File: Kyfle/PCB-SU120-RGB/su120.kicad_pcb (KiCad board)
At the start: 2 copper layers, 94 x 94 mm, 416 parts, among them J1 MJ-4PP-9, J2 Conn_01x03, J3 Conn_01x08, J4 Conn_01x08, J6 MJ-4PP-9, J7 Conn_02x05_Odd_Even, J8 Conn_02x05_Odd_Even, SW1 SW_PUSH_LED, SW10 SW_PUSH_LED, SW11 SW_PUSH_LED, SW12 SW_PUSH_LED, SW13 SW_PUSH_LED, SW14 SW_PUSH_LED, SW15 SW_PUSH_LED, SW16 SW_PUSH_LED, SW17 SW_PUSH_LED, SW18 SW_PUSH_LED, SW2 SW_PUSH_LED, SW20 Rotary_Encoder_Switch, SW21 Rotary_Encoder_Switch, SW22 SW_Push, SW3 SW_PUSH_LED, SW4 SW_PUSH_LED, SW5 SW_PUSH_LED, SW6 SW_PUSH_LED, SW7 SW_PUSH_LED, SW8 SW_PUSH_LED, SW9 SW_PUSH_LED, U1 ProMicro

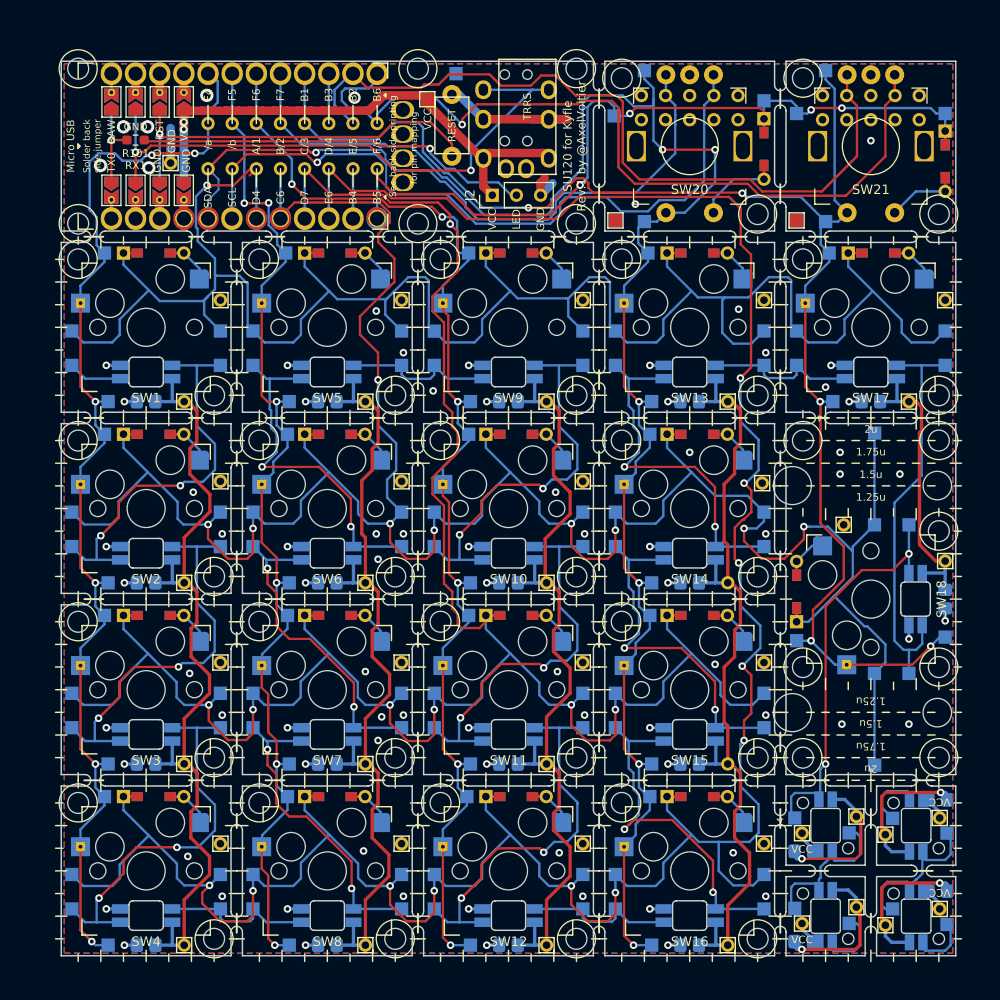
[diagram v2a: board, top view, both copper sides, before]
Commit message: Massive redesign
- Realised the design was not reversible. Only solution was to mirror the two diagonal holes of each bit. But one of them was coliding with hotswap socket footprint. Until...
- I also realised that having the holes at these Y positions made the screw coming on top collide with the bottom of the switch housing...
- So switched to having two holes right in between each bit (vertically).
- Then I realised cheap pcb houses can have quite some limitations when it comes to exotic uses of slots. In particular, for jlcpcb:
  * They prefer tabs to be >= 4mm wide
  * They prefer at least 3mm of PCB next to a slot (ie. avoid slim inter-slots parts)
  * They prefer 0.4mm clearence from board edge when it is milled/routed
  * Watching some videos of their fab it seems they do the edge.cuts routing with a single 1mm bit. Ie. if you specify a larger radius they actually route it out. And if you specify a smaller radius (than 0.5mm) they cannot do it.

So, I redid the PCB. Twice... Again. For now...

I also started reorganising the projects. First part was to gather all footprints used accross the three boards. Makes cross-board editing of footprints easier.
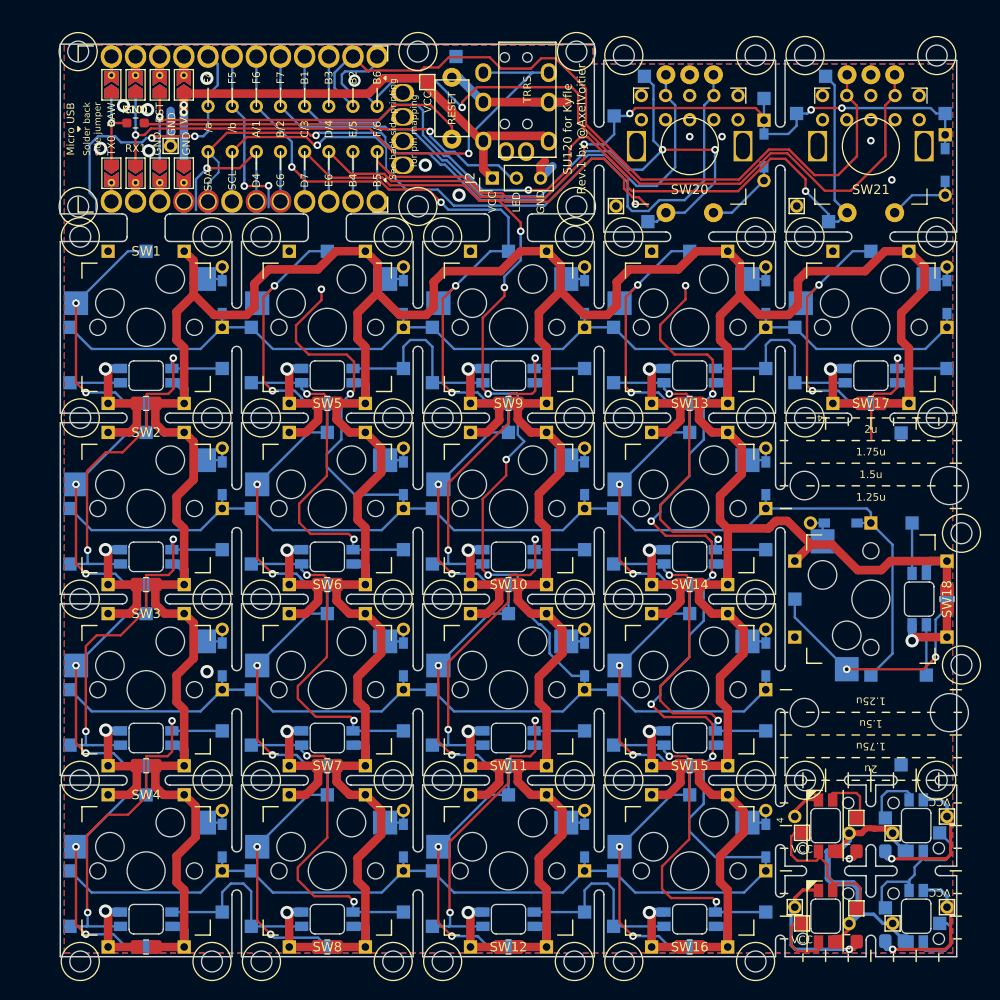
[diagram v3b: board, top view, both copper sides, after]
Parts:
- removed the ? at (120.7, 135.7)
- removed the ? at (134.9, 73.8)
- removed the ? at (120.7, 59.5)
- removed the ? at (101.6, 59.5)
- removed the ? at (70.6, 85.7)
- removed the ? at (89.7, 142.9)
- removed the ? at (108.7, 142.9)
- removed the ? at (127.8, 114.3)
- removed the ? at (51.6, 123.8)
- removed the ? at (70.6, 123.8)
- removed the ? at (89.7, 123.8)
- removed the ? at (108.7, 123.8)
- removed the ? at (70.6, 142.9)
- removed the ? at (51.6, 142.9)
- removed the ? at (108.7, 104.8)
- removed the ? at (89.7, 104.8)
- removed the ? at (70.6, 104.8)
- removed the ? at (51.6, 104.8)
- removed the ? at (51.6, 85.7)
- removed the ? at (89.7, 85.7)
- removed the ? at (127.8, 85.7)
- removed the ? at (125.4, 140.5)
- removed the ? at (108.7, 85.7)
- removed the ? at (80.6, 65.5)
- removed the ? at (83.7, 65.1)
- removed the ? at (125.4, 150.0)
- removed the ? at (120.7, 145.3)
- removed C1, C10, C11, C12, C13, C14, C15, C16, C17, C18, C2, C3, C4, C5, C6, C7, C8, C9: 100n, #footprint:C_0603_0805_HandSolder
- removed D1, D10, D11, D12, D13, D14, D15, D16, D17, D2, D20, D3, D4, D5, D6, D7, D8, D9: D, #footprint:diode_TH_SMD_rev2
- removed H1, H10, H100, H102, H104, H106, H108, H11, H110, H112, H113, H114, H115, H116, H117, H118, H119, H12, H120, H121, H122, H123, H124, H125, H126, H127, H128, H129, H13, H130, H131, H132, H14, H142, H145, H147, H149, H15, H151, H16, H17, H18, H19, H2, H20, H21, H210, H211, H212, H213, H22, H23, H24, H25, H26, H27, H28, H29, H3, H30, H31, H32, H33, H34, H35, H36, H37, H38, H39, H4, H40, H41, H42, H43, H44, H45, H47, H48, H49, H5, H51, H53, H55, H59, H6, H61, H63, H65, H67, H69, H7, H71, H72, H74, H76, H78, H8, H80, H82, H84, H87, H89, H9, H91, H93, H95, H97, H99: MountingHole_Pad, #footprint:1pad_conn
- removed H101, H103, H105, H107, H109, H111, H141, H143, H144, H146, H148, H150, H52, H54, H56, H58, H60, H62, H64, H66, H68, H70, H73, H75, H77, H79, H81, H83, H85, H86, H88, H90, H92, H94, H96, H98: MountingHole_Pad, #footprint:1pin_conn
- removed the REF** at (118.3, 66.7)
- removed the REF** at (80.2, 123.8)
- removed the REF** at (61.1, 123.8)
- removed the REF** at (61.1, 104.8)
- removed the REF** at (80.2, 104.8)
- removed the REF** at (99.2, 104.8)
- removed the REF** at (118.3, 85.7)
- removed the REF** at (99.2, 85.7)
- removed the REF** at (80.2, 85.7)
- removed the REF** at (61.1, 85.7)
- removed the REF** at (127.8, 95.2)
- removed the REF** at (99.2, 66.7)
- removed the REF** at (127.8, 76.2)
- removed the REF** at (108.7, 76.2)
- removed the REF** at (108.7, 95.2)
- removed the REF** at (108.7, 114.3)
- removed the REF** at (108.7, 133.3)
- removed the REF** at (89.7, 133.3)
- removed the REF** at (89.7, 114.3)
- removed the REF** at (89.7, 95.2)
- removed the REF** at (89.7, 76.2)
- removed the REF** at (70.6, 95.2)
- removed the REF** at (118.3, 104.8)
- removed the REF** at (70.6, 114.3)
- removed the REF** at (70.6, 133.3)
- removed the REF** at (51.6, 133.3)
- removed the REF** at (51.6, 114.3)
- removed the REF** at (51.6, 95.2)
- removed the REF** at (51.6, 76.2)
- removed the REF** at (118.3, 142.9)
- removed the REF** at (127.8, 133.3)
- removed the REF** at (127.8, 142.9)
- removed the REF** at (118.3, 123.8)
- removed the REF** at (70.6, 76.2)
- removed the REF** at (118.3, 133.3)
- removed the REF** at (118.3, 152.4)
- removed the REF** at (127.8, 152.4)
- removed the REF** at (61.1, 142.9)
- removed the REF** at (42.1, 95.2)
- removed the REF** at (80.2, 142.9)
- removed the REF** at (99.2, 142.9)
- removed the REF** at (99.2, 123.8)
- removed the Ref** at (134.9, 121.4)
- removed the Ref** at (82.5, 135.7)
- removed the Ref** at (101.6, 135.7)
- removed the Ref** at (101.6, 116.7)
- removed the Ref** at (82.5, 116.7)
- removed the Ref** at (63.5, 116.7)
- removed the Ref** at (44.5, 116.7)
- removed the Ref** at (44.5, 97.6)
- removed the Ref** at (63.5, 97.6)
- removed the Ref** at (82.5, 97.6)
- removed the Ref** at (101.6, 97.6)
- removed the Ref** at (134.9, 107.2)
- removed the Ref** at (120.7, 78.6)
- removed the Ref** at (101.6, 78.6)
- removed the Ref** at (82.5, 78.6)
- removed the Ref** at (63.5, 78.6)
- removed the Ref** at (44.5, 78.6)
- removed the Ref** at (58.7, 150.0)
- removed the Ref** at (77.8, 150.0)
- removed the Ref** at (96.8, 150.0)
- removed the Ref** at (115.9, 150.0)
- removed the Ref** at (115.9, 131.0)
- removed the Ref** at (120.7, 121.4)
- removed the Ref** at (96.8, 131.0)
- removed the Ref** at (77.8, 131.0)
- removed the Ref** at (58.7, 131.0)
- removed the Ref** at (58.7, 111.9)
- removed the Ref** at (77.8, 111.9)
- removed the Ref** at (96.8, 111.9)
- removed the Ref** at (115.9, 111.9)
- removed the Ref** at (134.9, 92.9)
- removed the Ref** at (115.9, 92.9)
- removed the Ref** at (96.8, 92.9)
- removed the Ref** at (120.7, 131.0)
- removed the Ref** at (77.8, 92.9)
- removed the Ref** at (58.7, 92.9)
- removed the Ref** at (134.9, 97.6)
- removed the Ref** at (120.7, 97.6)
- removed the Ref** at (44.5, 135.7)
- removed the Ref** at (63.5, 135.7)
- added ?: , Kyfle Footprints:M2_Hole_Standoff_Large_Cleareance, F.Cu at (115.7, 57.1)
- added ?: , Kyfle Footprints:M2_Hole_Standoff_Large_Cleareance, F.Cu at (120.9, 57.1)
- added ?: , Kyfle Footprints:M2_Hole_Standoff_Large_Cleareance, F.Cu at (134.7, 57.1)
- added ?: , Kyfle Footprints:M2_Hole_Standoff_Large_Cleareance, F.Cu at (134.7, 76.2)
- added ?: , Kyfle Footprints:M2_Hole_Standoff_Large_Cleareance, F.Cu at (120.9, 76.2)
- added ?: , Kyfle Footprints:M2_Hole_Standoff_Large_Cleareance, F.Cu at (101.8, 76.2)
- added ?: , Kyfle Footprints:M1.4_tapping_Hole, B.Cu at (120.7, 140.5)
- added ?: , Kyfle Footprints:M1.4_tapping_Hole, B.Cu at (120.7, 150.0)
- added ?: , Kyfle Footprints:M1.4_tapping_Hole, B.Cu at (125.4, 145.3)
- added ?: , Kyfle Footprints:M1.4_tapping_Hole, B.Cu at (125.4, 135.7)
- added ?: , Kyfle Footprints:M2_Hole_Standoff_Large_Cleareance, F.Cu at (96.6, 76.2)
- added ?: , , F.Cu at (80.6, 63.7)
- added ?: , , F.Cu at (83.7, 63.3)
- added ?: , Kyfle Footprints:M2_Hole_Standoff_Large_Cleareance, F.Cu at (82.8, 76.2)
- added ?: , Kyfle Footprints:M2_Hole_Standoff_Large_Cleareance, F.Cu at (77.6, 76.2)
- added ?: , Kyfle Footprints:M2_Hole_Standoff_Large_Cleareance, F.Cu at (63.7, 76.2)
- added ?: , Kyfle Footprints:M2_Hole_Standoff_Large_Cleareance, F.Cu at (58.5, 76.2)
- added ?: , Kyfle Footprints:M2_Hole_Standoff_Large_Cleareance, F.Cu at (44.7, 76.2)
- added ?: , Kyfle Footprints:M2_Hole_Standoff_Large_Cleareance, F.Cu at (101.8, 57.1)
- added REF**: Slot_1.2mm_9.75mm, Kyfle Footprints:Slot_Tee_1mm_2.7625mm, F.Cu at (127.8, 133.3)
- added REF**: Slot_1.2mm_9.75mm, Kyfle Footprints:Slot_Cross_1mm_2.7625mm, F.Cu at (127.8, 142.9)
- added REF**: Slot_1.2mm_3.7.mm, Kyfle Footprints:Slot_Half_Line_1mm_2.7625mm, F.Cu at (127.8, 152.4)
- added REF**: Slot_1.2mm_3.7.mm, Kyfle Footprints:Slot_Half_Line_1mm_2.7625mm, F.Cu at (118.3, 152.4)
- added REF**: Slot_1.2mm_3.7.mm, Kyfle Footprints:Slot_Half_Line_1mm_7.525mm, F.Cu at (42.1, 95.2)
- added REF** (x2): Slot_1.2mm_3.7.mm, Kyfle Footprints:Slot_Half_Line_1mm_2.7625mm, F.Cu at (118.3, 133.3)
- added REF** (x2): Slot_1.2mm_3.7.mm, Kyfle Footprints:Slot_Half_Line_1mm_7.525mm, F.Cu at (118.3, 133.3)
- added REF**: Slot_1.2mm_9.75mm, Kyfle Footprints:Slot_Tee_1mm_2.7625mm, F.Cu at (118.3, 142.9)
- added Ref**: Val**, Kyfle Footprints:M2_Hole_Standoff, F.Cu at (120.9, 133.3)
- ?: footprint #footprint:OLED_rivet -> Kyfle Footprints:OLED_Rivets
- ?: footprint #footprint:M2_Hole_Standoff -> Kyfle Footprints:M2_Hole_Standoff_Large_Cleareance
- ? (x4): footprint #footprint:M1.4_tapping_Hole -> Kyfle Footprints:M1.4_tapping_Hole
- ?: footprint #footprint:CherryMX_MidHeight_Choc_Hotswap_2U_Outline -> Kyfle Footprints:CherryMX_2U_Outline
- ? (x6), Ref**: footprint #footprint:M2_Hole_Standoff -> Kyfle Footprints:M2_Hole_Standoff
- ?: footprint #footprint:CherryMX_MidHeight_Choc_Silk -> Kyfle Footprints:CherryMX_MidHeight_Choc_Silk
- ? (x6): footprint #footprint:CherryMX_MidHeight_Choc_Silk_Line -> Kyfle Footprints:CherryMX_MidHeight_Choc_Silk_Line
- C19, C20: footprint #footprint:C_0603_0805_HandSolder -> Kyfle Footprints:C_0603_0805_HandSolder; moved to F.Cu
- C21, C22: footprint #footprint:C_0603_0805_HandSolder -> Kyfle Footprints:C_0603_0805_HandSolder
- D18, D19: footprint #footprint:diode_TH_SMD_rev2 -> Kyfle Footprints:diode_TH_SMD_rev3
- H133, H134, H135, H136, H137, H138, H139, H140, H161, H162, H165, H166, H168, H169, H46, H50: footprint #footprint:1pad_conn -> Kyfle Footprints:1pad_conn
- H152, H155, H156: footprint #footprint:1pin_conn -> Kyfle Footprints:1pin_conn; moved to F.Cu
- H153, H154, H157, H158: footprint #footprint:1pad_conn -> Kyfle Footprints:1pad_conn; moved to F.Cu
- H159, H160, H163, H164, H167, H57: footprint #footprint:1pin_conn -> Kyfle Footprints:1pin_conn
- H170, H171: footprint #footprint:1pad_conn -> Kyfle Footprints:1pin_conn; moved to B.Cu
- J1, J6: footprint #footprint:MJ-4PP-9 -> Kyfle Footprints:MJ-4PP-9
- J2: footprint #footprint:PinHeader_1x03_P2.54mm_Vertical -> Kyfle Footprints:PinHeader_1x03_P2.54mm_Vertical
- J3, J4: footprint #footprint:PinHeader_1x08_P2.54mm_Vertical_rev2 -> Kyfle Footprints:PinHeader_1x08_P2.54mm_Vertical_rev2
- J7, J8: footprint #footprint:IDC-Header_2x05_P2.54mm_Vertical -> Kyfle Footprints:IDC-Header_2x05_P2.54mm_Vertical
- JP101, JP102, JP103, JP104, JP105, JP106, JP107, JP108: footprint #footprint:SolderJumper-3_P1.3mm_Open_TrianglePad1.0x1.5mm_duplex -> Kyfle Footprints:SolderJumper-3_P1.3mm_Open_TrianglePad1.0x1.5mm_duplex
- LED1, LED2: footprint #footprint:SK6812_Mini_E -> Kyfle Footprints:SK6812_Mini_E; moved to F.Cu
- LED3, LED4: footprint #footprint:SK6812_Mini_E -> Kyfle Footprints:SK6812_Mini_E
- R101: value 50R -> 501R
- REF**: footprint #footprint:Slot_Cross_1.2mm_7.4mm -> Kyfle Footprints:Slot_Cross_2.9mm_7.525mm
- REF** (x2): footprint #footprint:Slot_Line_1.2mm_3.7mm -> Kyfle Footprints:Slot_Half_Line_1mm_2.7625mm
- REF** (x9): footprint #footprint:Slot_Line_1.2mm_3.7mm -> Kyfle Footprints:Slot_Half_Line_1mm_7.525mm
- REF** (x2): footprint #footprint:Slot_Tee_1.2mm_7.4mm -> Kyfle Footprints:Slot_Tee_2.9mm_7.525mm
- REF**: footprint #footprint:Slot_Tee_1.2mm_7.4mm -> Kyfle Footprints:Slot_Tee_1mm_7.525mm
- REF** (x6): footprint #footprint:Slot_Cross_1.2mm_7.4mm_6.85mm -> Kyfle Footprints:Slot_Cross_1mm_7.525mm
- REF** (x5): footprint #footprint:Slot_Cross_1.2mm_7.4mm -> Kyfle Footprints:Slot_Cross_1mm_7.525mm
- REF**: footprint #footprint:Slot_Line_1.2mm_3.7mm -> Kyfle Footprints:Slot_Half_Line_2.9mm_7.525mm
- SW1, SW10, SW11, SW12, SW13, SW14, SW15, SW16, SW17, SW18, SW2, SW3, SW4, SW5, SW6, SW7, SW8, SW9: footprint #footprint:CherryMX_MidHeight_RGB_Hotswap -> Kyfle Footprints:CherryMX_Kyfle_v1_Module
- SW20, SW21: footprint #footprint:RotaryEncoder_Alps_EC11E-Switch_Vertical_H20mm_rev2 -> Kyfle Footprints:RotaryEncoder_Alps_EC11E-Switch_Vertical_H20mm_rev2
- SW22: footprint #footprint:ResetSW -> Kyfle Footprints:ResetSW
- U1: footprint #footprint:ArduinoProMicro-Rivets -> Kyfle Footprints:Arduino_ProMicro_Rivets
- moved H46 25.4 mm to (131.0, 131.7), turned to 0 degrees
- moved H162 12.9 mm to (129.3, 137.3), turned to 180 degrees
- moved H165 12.1 mm to (135.0, 148.4), turned to 180 degrees
- moved H166 10.2 mm to (129.3, 146.8), turned to 180 degrees
- moved LED3 9.52 mm to (132.6, 138.1), turned to 270 degrees
- moved LED4 9.52 mm to (132.6, 147.6), turned to 270 degrees
- moved H161 9.41 mm to (135.0, 138.9), turned to 180 degrees
- moved C22 7.06 mm to (130.3, 140.8)
- moved C21 6.95 mm to (130.3, 150.3)
- moved H163 6.75 mm to (135.8, 146.7), turned to 180 degrees
- moved H167 6.75 mm to (135.8, 137.2), turned to 180 degrees
- moved ? 6.74 mm to (134.9, 140.5), turned to 180 degrees
- moved ? 6.74 mm to (134.9, 150.0), turned to 180 degrees
- moved ? 6.74 mm to (130.2, 135.7), turned to 180 degrees
- moved ? 6.74 mm to (130.2, 145.3), turned to 180 degrees
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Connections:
- C19 pad 1: VCC -> GND
- C19 pad 2: GND -> VCC
- C20 pad 1: VCC -> GND
- C20 pad 2: GND -> VCC
- C21 pad 1: VCC -> GND
- C21 pad 2: GND -> VCC
- C22 pad 1: VCC -> GND
- C22 pad 2: GND -> VCC
- J2 pad 2: Net-(J2-Pad2) -> led
- JP104 pad 1: led -> led_
- JP105 pad 3: led -> led_
- R101 pad 2: Net-(J2-Pad2) -> led_
- SW1 pad 4: Net-(H51-Pad1) -> led
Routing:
- net VCC: track 447.2 -> 692.9 mm
- net GND: track 141.5 -> 294.5 mm, vias 86 -> 36
- net Y2: track 279.4 -> 158.3 mm, vias 9 -> 2
- net Y1: track 225.2 -> 125.1 mm
- net Y4: track 289.9 -> 220.5 mm, vias 11 -> 6
- net Y3: track 233.9 -> 179.5 mm, vias 7 -> 5
- net Net-(J2-Pad2): track 41.8 -> 0.00 mm, vias 1 -> 0
- net led: track 9.07 -> 47.1 mm
- net Net-(H154-Pad1): track 42.7 -> 11.5 mm, vias 2 -> 0
- net X3: track 132.7 -> 157.5 mm, vias 6 -> 10
- net Net-(SW17-Pad2): track 43.2 -> 22.4 mm, vias 0 -> 1
- net X1: track 128.6 -> 143.8 mm, vias 6 -> 10
- net X2: track 121.1 -> 133.7 mm, vias 6 -> 10
- net X5: track 161.5 -> 151.0 mm, vias 5 -> 6
- net led_: track 0.00 -> 9.07 mm, vias 0 -> 1
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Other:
- board size 94 x 94 mm -> 94.2 x 95.9 mm
- net class PWR: clearance 0.2 -> 0.1524

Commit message: PCB done. Started redoing the rails.
- PCB should be in its final version now, pretty much. I hope...
- I added a tentative compatibility with Panasonic roller encoders.
- Also added some silk screens for the 2u stabilisers.
- Propagated the new bit board design to footprints used for top and bottom plate.
- And started to rework the rails in the bottom plate, as well as the general shape of the keyboard.
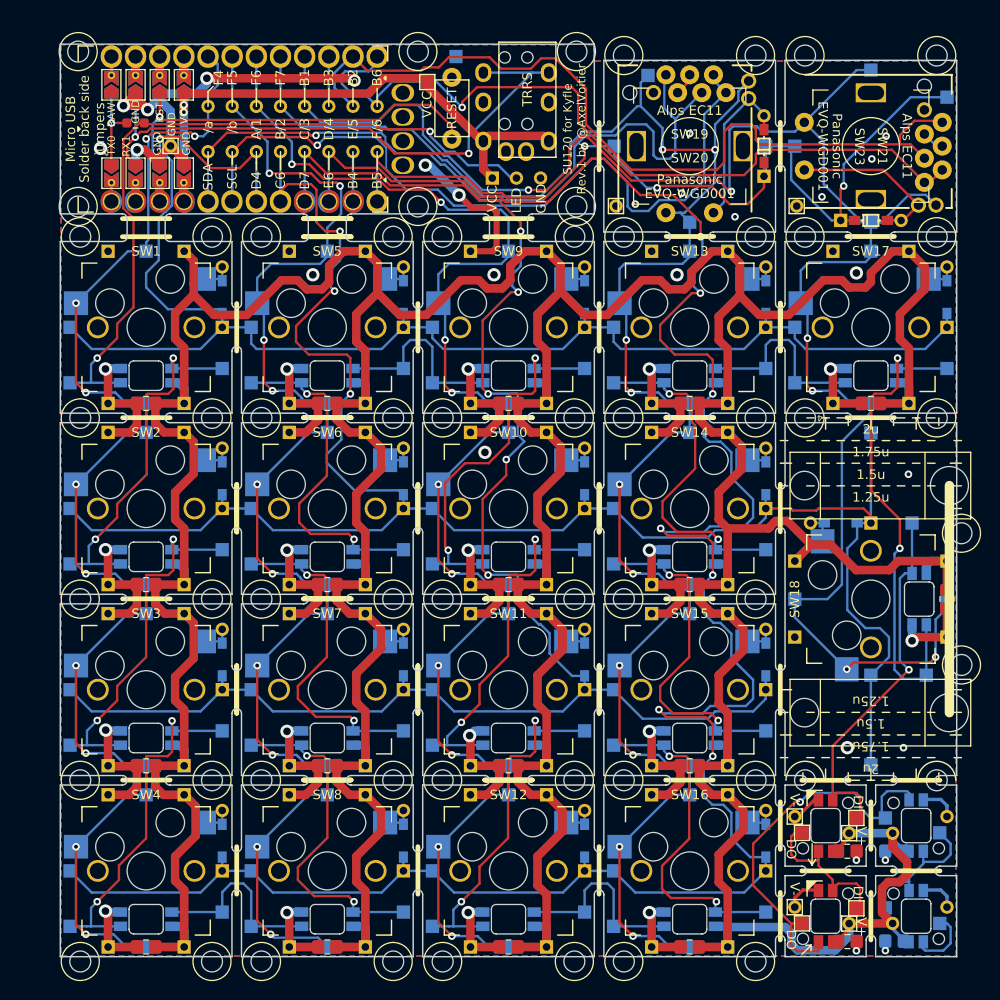
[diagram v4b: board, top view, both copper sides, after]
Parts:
- removed the ? at (127.8, 142.9)
- removed J7, J8: Conn_02x05_Odd_Even, Kyfle Footprints:IDC-Header_2x05_P2.54mm_Vertical
- added SW19: Rotary_Encoder_Switch, Kyfle Footprints:RollerEncoder_Panasonic_EVQWGD001_No_Cutout, F.Cu at (108.7, 66.7)
- added SW23: Rotary_Encoder_Switch, Kyfle Footprints:RollerEncoder_Panasonic_EVQWGD001_No_Cutout, F.Cu at (127.8, 66.7)
- D18, D19, H152, H155, H156: moved to B.Cu
- H160, H163, H164, H167: moved to F.Cu
- Ref** (x2): footprint Kyfle Footprints:M2_Hole_Standoff -> Kyfle Footprints:M2_Hole_Standoff_Default_Cleareance_Half_Silk
- moved D19 11.9 mm to (127.8, 74.5), turned to 0 degrees
- moved H138 5.02 mm to (116.7, 66.7)
- moved H134 4.81 mm to (127.8, 58.7)
- moved ? 4.76 mm to (127.8, 66.7)
- moved H136 4.45 mm to (127.8, 74.7)
- moved H135 4.40 mm to (108.7, 74.7)
- moved H139 3.43 mm to (119.8, 66.7)
- moved ? 3.17 mm to (108.7, 66.7)
- moved H137 3.17 mm to (100.8, 66.7)
- moved H46 3.17 mm to (127.8, 131.7)
- moved H50 3.17 mm to (127.8, 96.8)
- moved D18 2.72 mm to (116.6, 66.7), turned to 90 degrees
- moved ? 2.48 mm to (106.5, 66.7), turned to 105 degrees
- moved H140 1.73 mm to (135.8, 61.5)
- moved ? 0.51 mm to (127.8, 64.0), turned to 15 degrees
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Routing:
- net X5: track 151.0 -> 193.3 mm
- net Y2: track 158.3 -> 199.2 mm, vias 2 -> 3
- net Y1: track 125.1 -> 156.3 mm
- net led: track 47.1 -> 77.9 mm, vias 1 -> 2
- net Y4: track 220.5 -> 250.8 mm, vias 6 -> 7
- net Net-(SW17-Pad2): track 22.4 -> 52.0 mm, vias 1 -> 2
- net Net-(H154-Pad1): track 11.5 -> 39.6 mm, vias 0 -> 1
- net Net-(H157-Pad1): track 13.5 -> 41.5 mm, vias 0 -> 1
- net VCC: track 692.9 -> 709.8 mm
- net Y6: track 83.5 -> 96.1 mm, vias 4 -> 3
- net X4: track 194.6 -> 205.8 mm
- net X2: track 133.7 -> 143.9 mm
- net Net-(D19-Pad2): track 7.52 -> 17.7 mm
- net Net-(D18-Pad2): track 8.16 -> 17.6 mm
- net GND: track 294.5 -> 303.1 mm, vias 36 -> 45
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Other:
- board text added: "DI"
- board text added: "DO"
- board text added: "Solder back side jumpers"
- board text added: "V+"
- board text added: "V-"
- board text removed: "DIN"
- board text removed: "DOUT"
- board text removed: "See back side printing"
- board text removed: "Solder back side jumper"
- board text removed: "for pin mapping"

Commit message: Resized M2 slots and holes to 2mm instead of 2.2mm
After receiving M2 hardware, I noticed 2mm opening would provide a tighter and less wobbly fit than the typical M2 clearance of 2.2mm.

Also, finished the silkscreen of bottom plate, as well as M2 holes for encoders in top plate.
At this point, both top and bottom plate could be considered finished.
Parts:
- D18, D19: moved to F.Cu
- moved D18 4.19 mm to (112.4, 66.7)
- moved D19 4.19 mm to (127.8, 70.3)
- moved ? 2.04 mm to (42.4, 56.7)
- moved ? 2.04 mm to (42.4, 73.0)
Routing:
- net X5: track 193.3 -> 189.0 mm
- net X7: track 88.4 -> 85.7 mm
- net Y6: track 96.1 -> 93.6 mm
- net Net-(D19-Pad2): track 17.7 -> 15.4 mm
- net Net-(D18-Pad2): track 17.6 -> 15.9 mm
- net X4: track 205.8 -> 207.4 mm
- net X8: track 83.2 -> 84.2 mm
- net GND: vias 45 -> 46
